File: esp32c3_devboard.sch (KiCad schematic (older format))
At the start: 37 parts, among them J1 UART USB, J2 JTAG USB, J3 Conn_01x15_Male, J4 Conn_01x15_Male, SW1 RST, SW2 BOOT, U1 ESP32-C3-MINI-1, U2 SRV05-4, U3 AMS1117-3.3, U4 CP2102N-A01-GQFN28

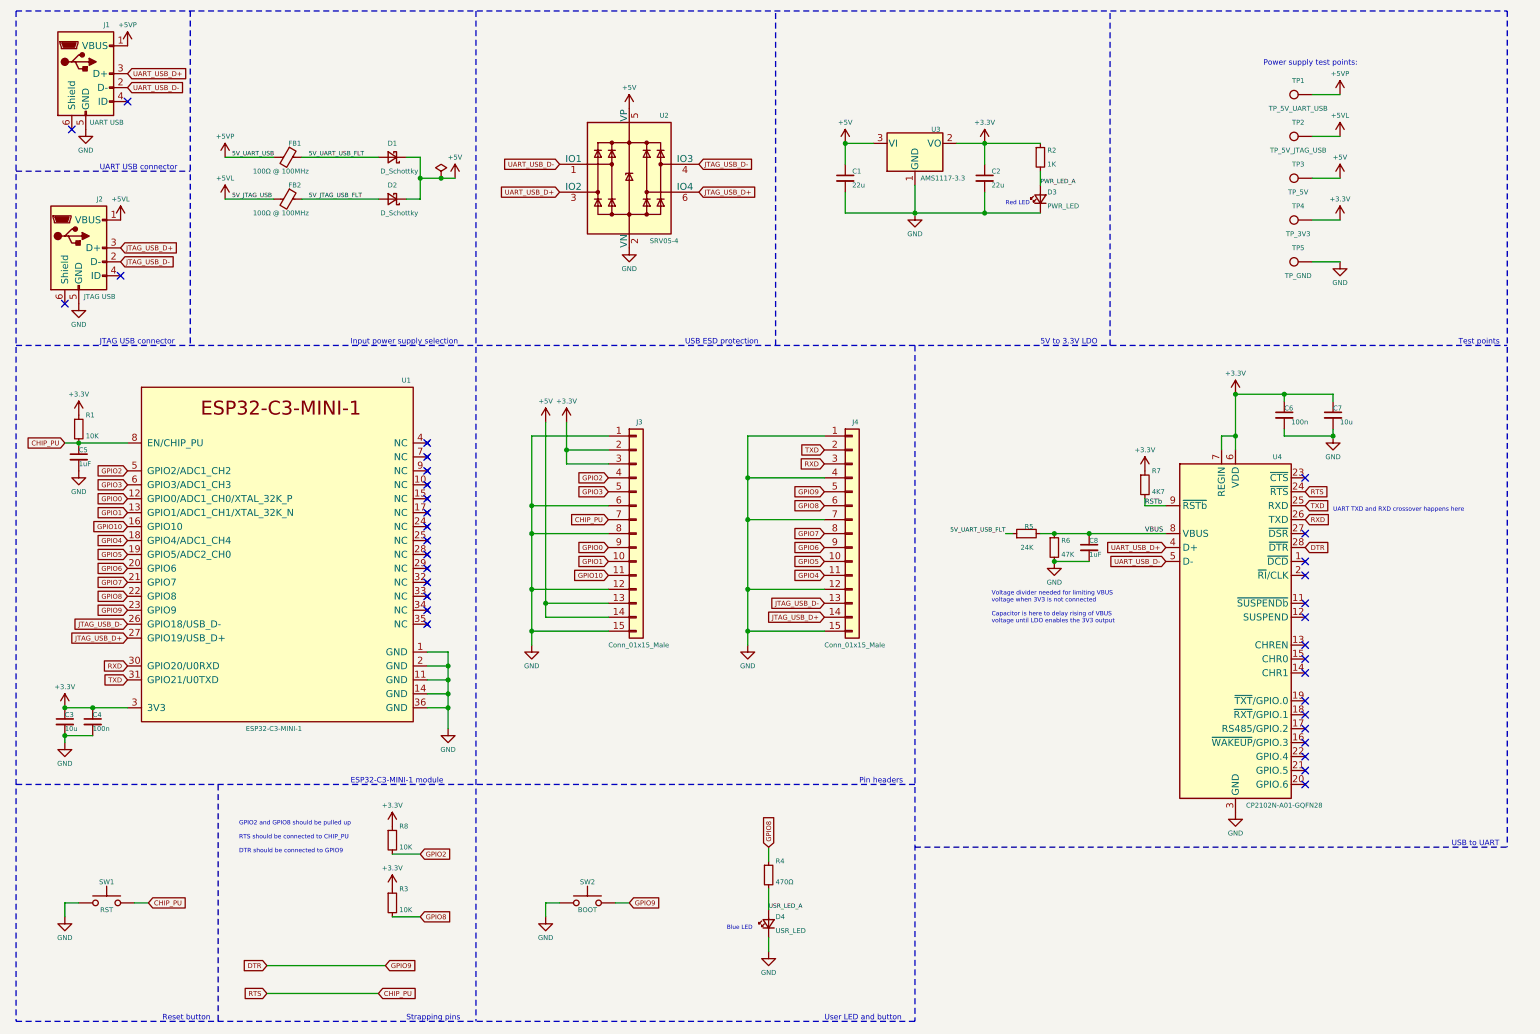
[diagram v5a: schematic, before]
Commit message: Add Microchip USB2514Bi USB hub to schematic and PCB
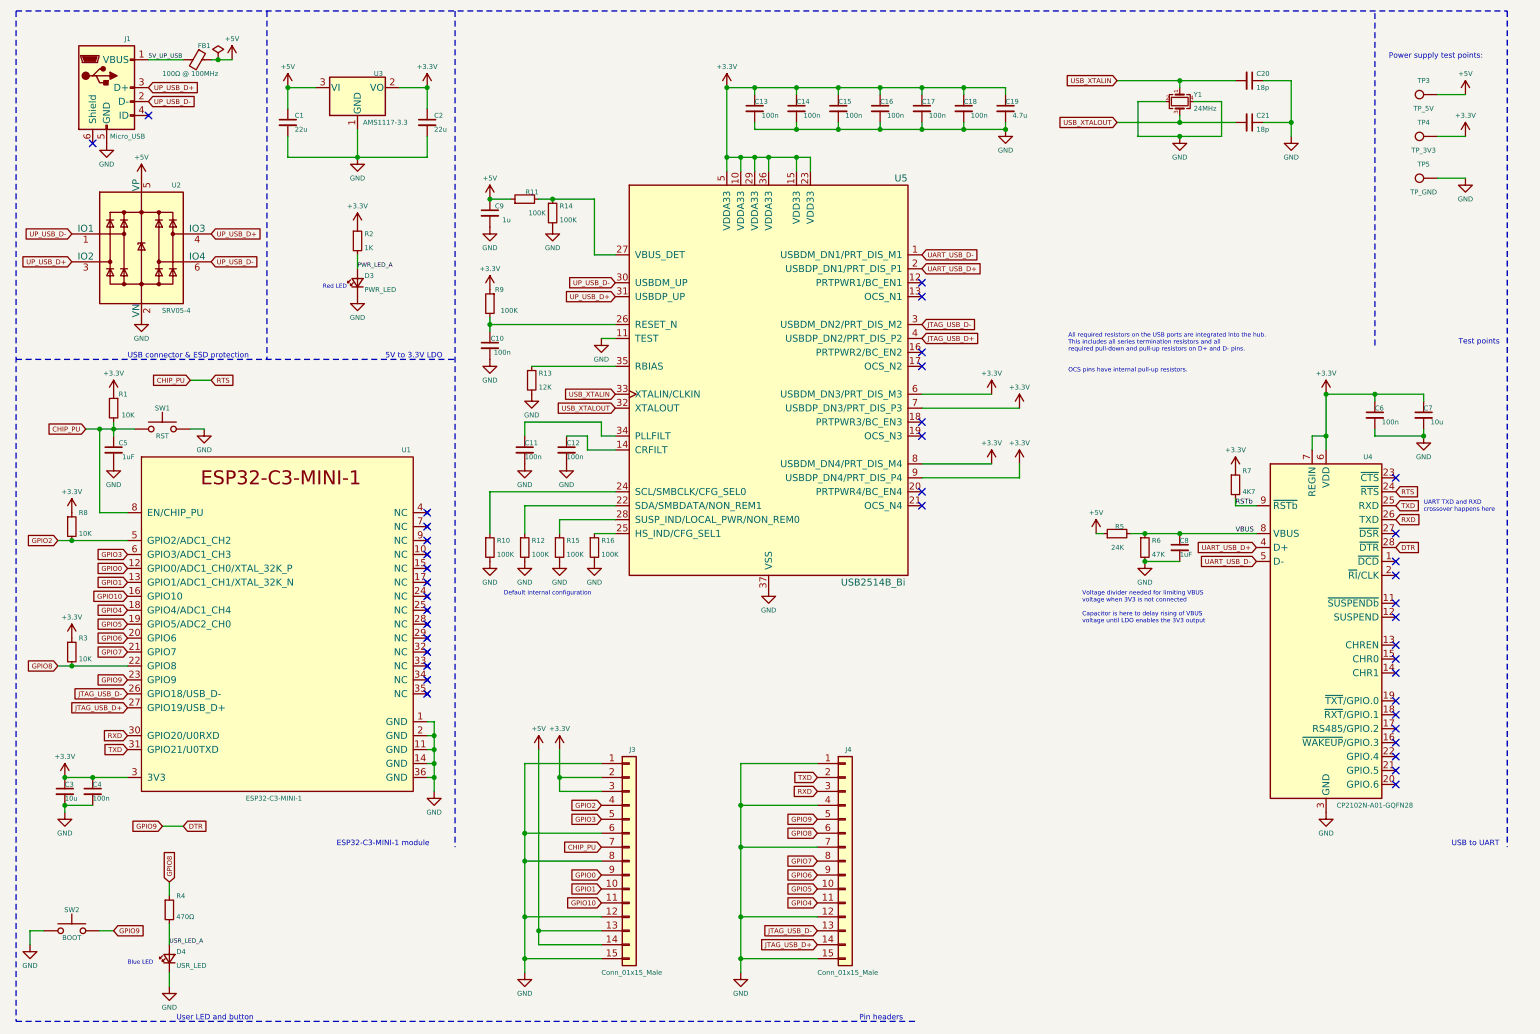
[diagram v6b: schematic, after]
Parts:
- removed D1, D2: D_Schottky, Diode_SMD:D_SOD-323, symbol Device:D_Schottky_Small
- removed FB2: 100Ω @ 100MHz, Inductor_SMD:L_0805_2012Metric, symbol Device:Ferrite_Bead_Small
- removed J2: JTAG USB, Connector_USB:USB_Micro-B_Wuerth_629105150521, symbol Connector:USB_B_Micro
- removed TP1: TP_5V_UART_USB, TestPoint:TestPoint_Pad_D1.0mm, symbol Connector:TestPoint
- removed TP2: TP_5V_JTAG_USB, TestPoint:TestPoint_Pad_D1.0mm, symbol Connector:TestPoint
- added C10, C11, C12, C13, C14, C15, C16, C17, C18: 100n, Capacitor_SMD:C_0402_1005Metric, symbol Device:C_Small
- added C19: 4.7u, Capacitor_SMD:C_0603_1608Metric, symbol Device:C_Small
- added C20, C21: 18p, Capacitor_SMD:C_0201_0603Metric, symbol Device:C_Small
- added C9: 1u, Capacitor_SMD:C_0402_1005Metric, symbol Device:C_Small
- added R10, R11, R12, R14, R15, R16, R9: 100K, Resistor_SMD:R_0402_1005Metric, symbol Device:R_Small
- added R13: 12K, Resistor_SMD:R_0402_1005Metric, symbol Device:R_Small
- added U5: USB2514B_Bi, Package_DFN_QFN:QFN-36-1EP_6x6mm_P0.5mm_EP3.7x3.7mm, symbol Interface_USB:USB2514B_Bi
- added Y1: 24MHz, Crystal:Crystal_SMD_2016-4Pin_2.0x1.6mm, symbol Device:Crystal_GND24_Small
- C1, C2: footprint Capacitor_SMD:C_1206_3216Metric -> Capacitor_SMD:C_0805_2012Metric
- C3, C7: footprint Capacitor_SMD:C_0805_2012Metric -> Capacitor_SMD:C_0603_1608Metric
- J1: value UART USB -> Micro_USB
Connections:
- net 5V_UART_USB_FLT is gone; now on net +5V: FB1.1, R5.1
- net +3V3: now also C13.1, C14.1, C15.1, C16.1, C17.1, C18.1, C19.1, R9.1, U5.10 (VDDA33), U5.15 (VDD33), U5.23 (VDD33), U5.29 (VDDA33), U5.36 (VDDA33), U5.5 (VDDA33), U5.6 (USBDM_DN3/PRT_DIS_M3), U5.7 (USBDP_DN3/PRT_DIS_P3), U5.8 (USBDM_DN4/PRT_DIS_M4), U5.9 (USBDP_DN4/PRT_DIS_P4)
- net +5V: now also C9.1, R11.1
- net GND: now also C10.2, C11.2, C12.2, C13.2, C14.2, C15.2, C16.2, C17.2, C18.2, C19.2, C20.1, C21.1, C9.2, R10.2, R12.2, R13.2, R14.2, R15.2, R16.2, U5.11 (TEST), U5.37 (VSS), Y1.2, Y1.4
- net JTAG_USB_D+: now also U5.4 (USBDP_DN2/PRT_DIS_P2); no longer U2.6 (IO4)
- net JTAG_USB_D-: now also U5.3 (USBDM_DN2/PRT_DIS_M2); no longer U2.4 (IO3)
- net UART_USB_D+: now also U5.2 (USBDP_DN1/PRT_DIS_P1); no longer J1.3 (D+), U2.3 (IO2)
- net UART_USB_D-: now also U5.1 (USBDM_DN1/PRT_DIS_M1); no longer J1.2 (D-), U2.1 (IO1)
- net +5VP renamed 5V_UP_USB
- new net: C12.1, U5.14 (CRFILT)
- new net: R12.1, U5.22 (SDA/SMBDATA/NON_REM1)
- new net: R10.1, U5.24 (SCL/SMBCLK/CFG_SEL0)
- new net: R16.1, U5.25 (HS_IND/CFG_SEL1)
- new net: C10.1, R9.2, U5.26 (RESET_N)
- new net: R11.2, R14.1, U5.27 (VBUS_DET)
- new net: R15.1, U5.28 (SUSP_IND/LOCAL_PWR/NON_REM0)
- new net: C11.1, U5.34 (PLLFILT)
- new net: R13.1, U5.35 (RBIAS)
- new net UP_USB_D+: J1.3 (D+), U2.3 (IO2), U2.4 (IO3), U5.31 (USBDP_UP)
- new net UP_USB_D-: J1.2 (D-), U2.1 (IO1), U2.6 (IO4), U5.30 (USBDM_UP)
- new net USB_XTALIN: C20.2, U5.33 (XTALIN/CLKIN), Y1.1
- new net USB_XTALOUT: C21.2, U5.32 (XTALOUT), Y1.3
- no-connect marks 34 -> 40
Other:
- note added: "All required resistors on the USB ports are integrated into the hub.\nThis includes all series termination resistors and all\nrequired pull-down and pull-up resistors on D+ and D- pins."
- note added: "Default internal configuration"
- note added: "OCS pins have internal pull-up resistors."
- note added: "UART TXD and RXD\ncrossover happens here"
- note added: "USB connector & ESD protection"
- note removed: "GPIO2 and GPIO8 should be pulled up\n\nRTS should be connected to CHIP_PU\n\nDTR should be connected to GPIO9"
- note removed: "Input power supply selection"
- note removed: "JTAG USB connector"
- note removed: "Reset button"
- note removed: "Strapping pins"
- note removed: "UART TXD and RXD crossover happens here"
- note removed: "UART USB connector"
- note removed: "USB ESD protection"
- moved on the sheet: C1, C2, C3, C4, C5, C6, C7, C8, D3, D4, FB1, J1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

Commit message: Configure bootstrapping pins on USB hub IC
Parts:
- added C22: 100n, Capacitor_SMD:C_0402_1005Metric, symbol Device:C_Small
- added R17: 330R, Resistor_SMD:R_0402_1005Metric, symbol Device:R_Small
- added R18, R19, R20, R21: 10K, Resistor_SMD:R_0402_1005Metric, symbol Device:R_Small
- C10: value 100n -> 220n
- C19: value 4.7u -> 1u
- C20, C21: footprint Capacitor_SMD:C_0201_0603Metric -> Capacitor_SMD:C_0402_1005Metric
- R12, R15: value 100K -> 10K
- R13: value 12K -> 12K,1%
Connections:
- net +3V3: now also R12.1, R15.1, R18.2, R19.2, R20.2, R21.2; no longer U5.6 (USBDM_DN3/PRT_DIS_M3), U5.7 (USBDP_DN3/PRT_DIS_P3), U5.8 (USBDM_DN4/PRT_DIS_M4), U5.9 (USBDP_DN4/PRT_DIS_P4)
- net +5V: now also R11.2; no longer R11.1
- net GND: now also R10.1, R16.1, C22.2, R17.1; no longer R10.2, R12.2, R15.2, R16.2
- net at J1.6 (Shield): now also C22.1, R17.2
- net NON_REM1: now reaches U5.22 (SDA/SMBDATA/NON_REM1)
- net NON_REM1: now also R15.2; no longer R12.1
- net CFG_SEL0: now reaches U5.24 (SCL/SMBCLK/CFG_SEL0)
- net CFG_SEL0: now also R10.2; no longer R10.1
- net CFG_SEL1: now reaches U5.25 (HS_IND/CFG_SEL1)
- net CFG_SEL1: now also R12.2; no longer R16.1
- net at R14.1, U5.27 (VBUS_DET): now also R11.1; no longer R11.2
- net NON_REM0: now reaches U5.28 (SUSP_IND/LOCAL_PWR/NON_REM0)
- net NON_REM0: now also R16.2; no longer R15.1
- new net: R18.1, U5.6 (USBDM_DN3/PRT_DIS_M3)
- new net: R20.1, U5.7 (USBDP_DN3/PRT_DIS_P3)
- new net: R19.1, U5.8 (USBDM_DN4/PRT_DIS_M4)
- new net: R21.1, U5.9 (USBDP_DN4/PRT_DIS_P4)
- no-connect marks 40 -> 39
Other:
- note added: "BC_EN pins have internal pull-down resistors"
- note added: "Default internal configuration, bus powered"
- note added: "Downstream ports 1 and 2 are non-removable"
- note added: "If unused, downstream USB ports need to be pulled up"
- note added: "Microchip\nrecommendation:"
- note added: "OCS_N pins have internal pull-up resistors"
- note added: "Silicon errata recommends\n220 nF on reset pin"
- note added: "Strapping pins:"
- note removed: "Default internal configuration"
- note removed: "OCS pins have internal pull-up resistors."
- moved on the sheet: C12, C9, FB1, J1, R10, R11
